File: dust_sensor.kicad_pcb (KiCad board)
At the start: 2 copper layers, 50 x 45 mm, 33 parts, among them P1 ADC, P10 PWR, P2 POWER, P3 LCD, P4 LCD_RST, P5 SERIAL, P6 DHT, P7 SENSOR, P8 GPIOS, P9 DEEP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

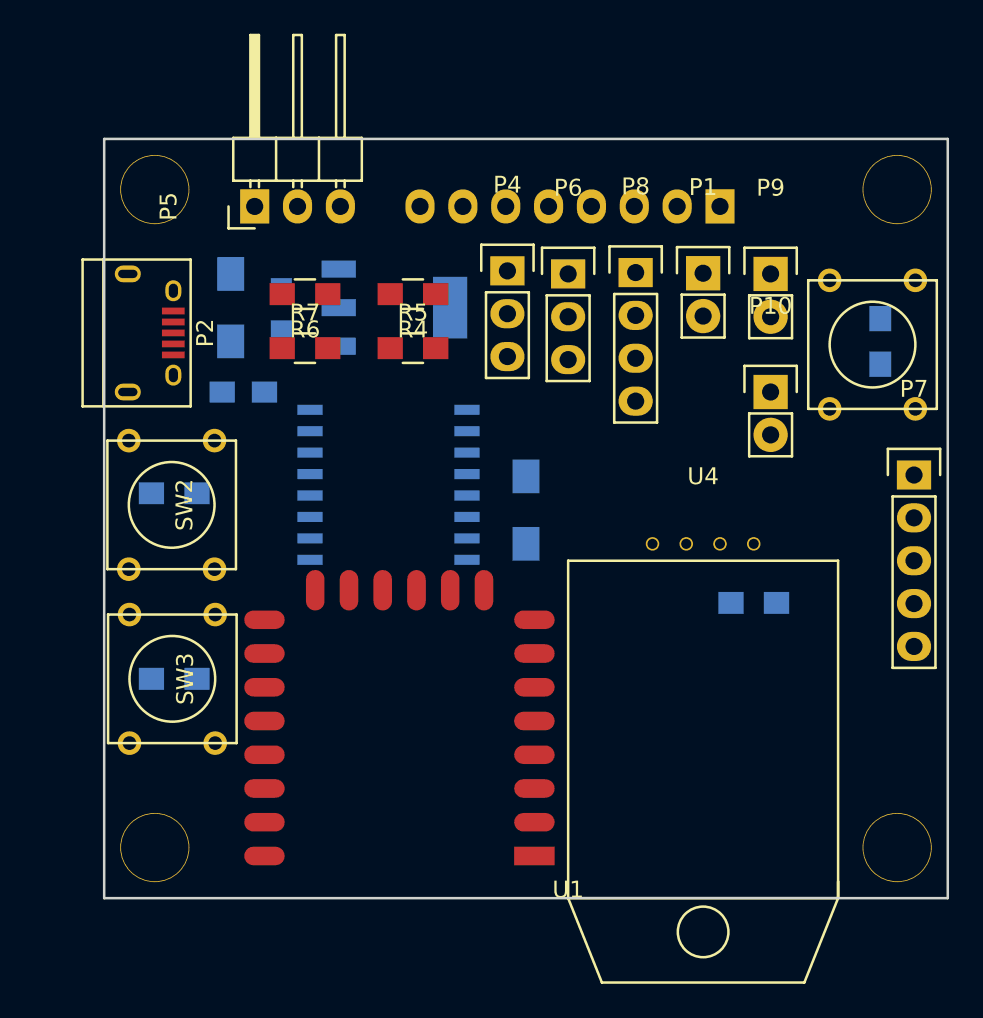
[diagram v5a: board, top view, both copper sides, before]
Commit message: SCH, PCB: remove 100uF from 1117 output
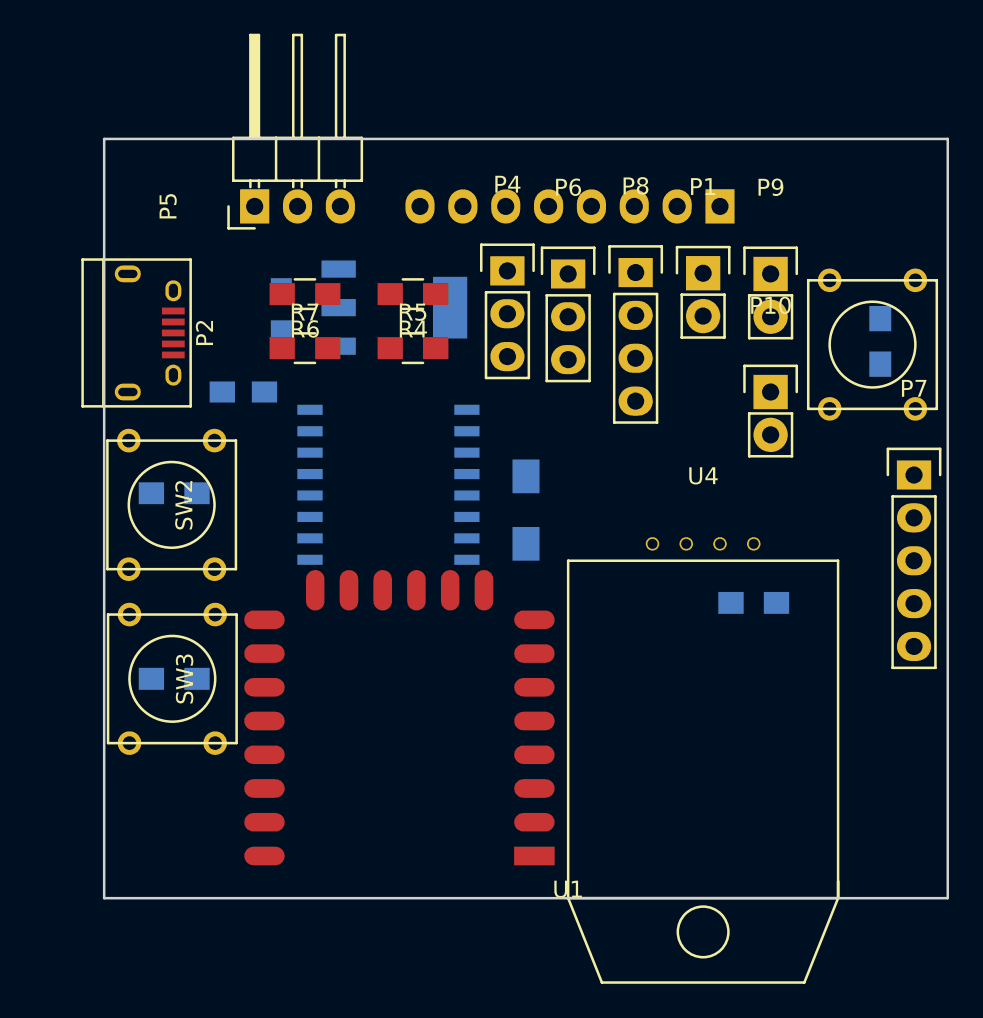
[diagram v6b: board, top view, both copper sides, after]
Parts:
- removed ? (x4): , dht:hole_4mm
- removed C3: 100u, Capacitors_SMD:C_1206_HandSoldering
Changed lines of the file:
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@@
 (kicad_pcb (version 4) (host pcbnew no-vcs-found-product)
   (general
-    (links 81)
-    (no_connects 81)
+    (links 79)
+    (no_connects 79)
     (area 39.424999 30.924999 89.575001 76.075001)
     (thickness 1.6)
@@
     (tracks 0)
     (zones 0)
-    (modules 33)
+    (modules 28)
     (nets 31)
   )
@@
       (net 2 GND))
     (model Capacitors_SMD.3dshapes/C_0805_HandSoldering.wrl
-      (at (xyz 0 0 0))
-      (scale (xyz 1 1 1))
-      (rotate (xyz 0 0 0))
-    )
-  )
-  (module Capacitors_SMD:C_1206_HandSoldering (layer B.Cu)
-    (at 47 41 270)
-    (descr "Capacitor SMD 1206, hand soldering")
-    (tags "capacitor 1206")
-    (attr smd)
-    (fp_text reference C3 (at 0 2.3 270) (layer B.SilkS)
-      (effects (font (size 1 1) (thickness 0.15)) (justify mirror))
-    )
-    (fp_text value 100u (at 0 -2.3 270) (layer B.Fab)
-      (effects (font (size 1 1) (thickness 0.15)) (justify mirror))
-    )
-    (fp_line (start -3.3 1.15) (end 3.3 1.15) (layer B.CrtYd) (width 0.05))
-    (fp_line (start -3.3 -1.15) (end 3.3 -1.15) (layer B.CrtYd) (width 0.05))
-    (fp_line (start -3.3 1.15) (end -3.3 -1.15) (layer B.CrtYd) (width 0.05))
-    (fp_line (start 3.3 1.15) (end 3.3 -1.15) (layer B.CrtYd) (width 0.05))
-    (fp_line (start 1 1.025) (end -1 1.025) (layer B.SilkS) (width 0.15))
-    (fp_line (start -1 -1.025) (end 1 -1.025) (layer B.SilkS) (width 0.15))
-    (pad 1 smd rect (at -2 0 270) (size 2 1.6) (layers B.Cu B.Paste B.Mask)
-      (net 1 +3V3))
-    (pad 2 smd rect (at 2 0 270) (size 2 1.6) (layers B.Cu B.Paste B.Mask)
-      (net 2 GND))
-    (model Capacitors_SMD.3dshapes/C_1206_HandSoldering.wrl
       (at (xyz 0 0 0))
       (scale (xyz 1 1 1))
@@
     )
   )
-  (module dht:hole_4mm (layer F.Cu)
-    (at 86.5 34)
-    (fp_text reference "" (at 0 0.5) (layer F.SilkS) hide
-      (effects (font (size 1 1) (thickness 0.15)))
-    )
-    (fp_text value "" (at 0 -0.5) (layer F.Fab) hide
-      (effects (font (size 1 1) (thickness 0.15)))
-    )
-    (pad 1 thru_hole circle (at 0 0) (size 4.1 4.1) (drill 4) (layers *.Cu *.Mask F.SilkS))
-  )
-  (module dht:hole_4mm (layer F.Cu)
-    (at 42.5 34)
-    (fp_text reference "" (at 0 0.5) (layer F.SilkS) hide
-      (effects (font (size 1 1) (thickness 0.15)))
-    )
-    (fp_text value "" (at 0 -0.5) (layer F.Fab) hide
-      (effects (font (size 1 1) (thickness 0.15)))
-    )
-    (pad 1 thru_hole circle (at 0 0) (size 4.1 4.1) (drill 4) (layers *.Cu *.Mask F.SilkS))
-  )
-  (module dht:hole_4mm (layer F.Cu)
-    (at 42.5 73)
-    (fp_text reference "" (at 0 0.5) (layer F.SilkS) hide
-      (effects (font (size 1 1) (thickness 0.15)))
-    )
-    (fp_text value "" (at 0 -0.5) (layer F.Fab) hide
-      (effects (font (size 1 1) (thickness 0.15)))
-    )
-    (pad 1 thru_hole circle (at 0 0) (size 4.1 4.1) (drill 4) (layers *.Cu *.Mask F.SilkS))
-  )
-  (module dht:hole_4mm (layer F.Cu)
-    (at 86.5 73)
-    (fp_text reference "" (at 0 0.5) (layer F.SilkS) hide
-      (effects (font (size 1 1) (thickness 0.15)))
-    )
-    (fp_text value "" (at 0 -0.5) (layer F.Fab) hide
-      (effects (font (size 1 1) (thickness 0.15)))
-    )
-    (pad 1 thru_hole circle (at 0 0) (size 4.1 4.1) (drill 4) (layers *.Cu *.Mask F.SilkS))
-  )
   (module Capacitors_SMD:C_0805_HandSoldering (layer B.Cu)

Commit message: PCB: some better component organization.
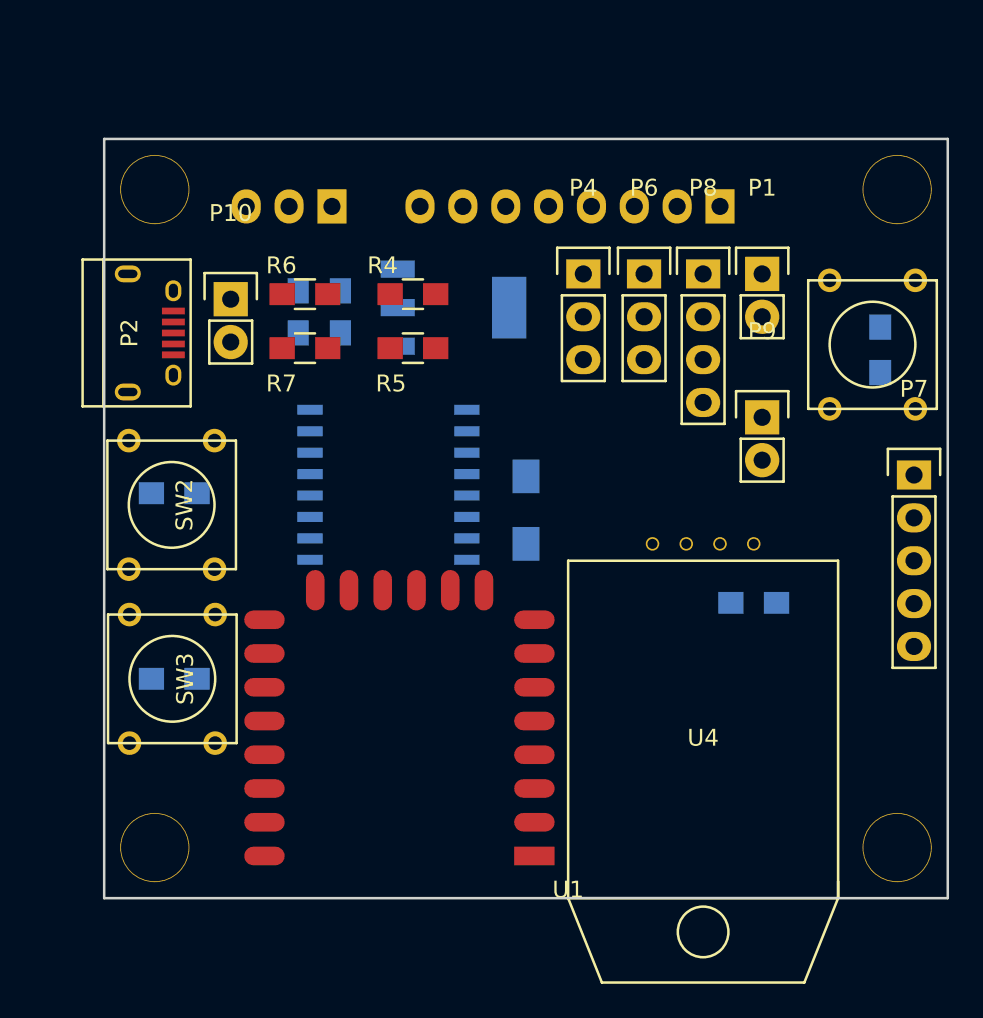
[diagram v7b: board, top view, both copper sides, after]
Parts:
- added ?: , dht:hole_4mm, F.Cu at (42.5, 34.0)
- added ?: , dht:hole_4mm, F.Cu at (86.5, 34.0)
- added ?: , dht:hole_4mm, F.Cu at (86.5, 73.0)
- added ?: , dht:hole_4mm, F.Cu at (42.5, 73.0)
- P5: moved to B.Cu
- moved P10 32.5 mm to (47.0, 40.5)
- moved P9 8.51 mm to (78.5, 47.5)
- moved C4 5.76 mm to (51.0, 41.2), turned to 270 degrees
- moved P5 4.58 mm to (53.0, 35.0)
- moved P4 4.50 mm to (67.9, 39.0)
- moved P6 4.50 mm to (71.5, 39.0)
- moved P8 4.00 mm to (75.0, 39.0)
- moved P1 3.50 mm to (78.5, 39.0)
- moved C2 3.50 mm to (53.5, 41.2)
- moved U2 3.50 mm to (60.2, 41.0)
- moved R1 0.50 mm to (85.5, 43.5)

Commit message: PCB: place some wires
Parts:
- turned C2 to 270 degrees
- turned R1 to 90 degrees
- turned R7 to 180 degrees
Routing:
- net GND: track 0.00 -> 127.0 mm
- net +3V3: track 0.00 -> 78.4 mm
- net RESET: track 0.00 -> 75.7 mm
- net TX: track 0.00 -> 54.2 mm
- net +5V: track 0.00 -> 54.0 mm, vias 0 -> 3
- net RX: track 0.00 -> 51.0 mm
- net ADC: track 0.00 -> 35.2 mm
- net GPIO16: track 0.00 -> 29.6 mm, vias 0 -> 1
- net SET: track 0.00 -> 26.4 mm
- net Net-(P1-Pad1): track 0.00 -> 20.8 mm
- net Net-(C2-Pad1): track 0.00 -> 12.8 mm, vias 0 -> 1
- net PROG: track 0.00 -> 10.3 mm
- net Net-(P6-Pad2): track 0.00 -> 4.69 mm, vias 0 -> 1
